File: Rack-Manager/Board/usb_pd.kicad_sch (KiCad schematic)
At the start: 1 part, among them U11 TPS25730D

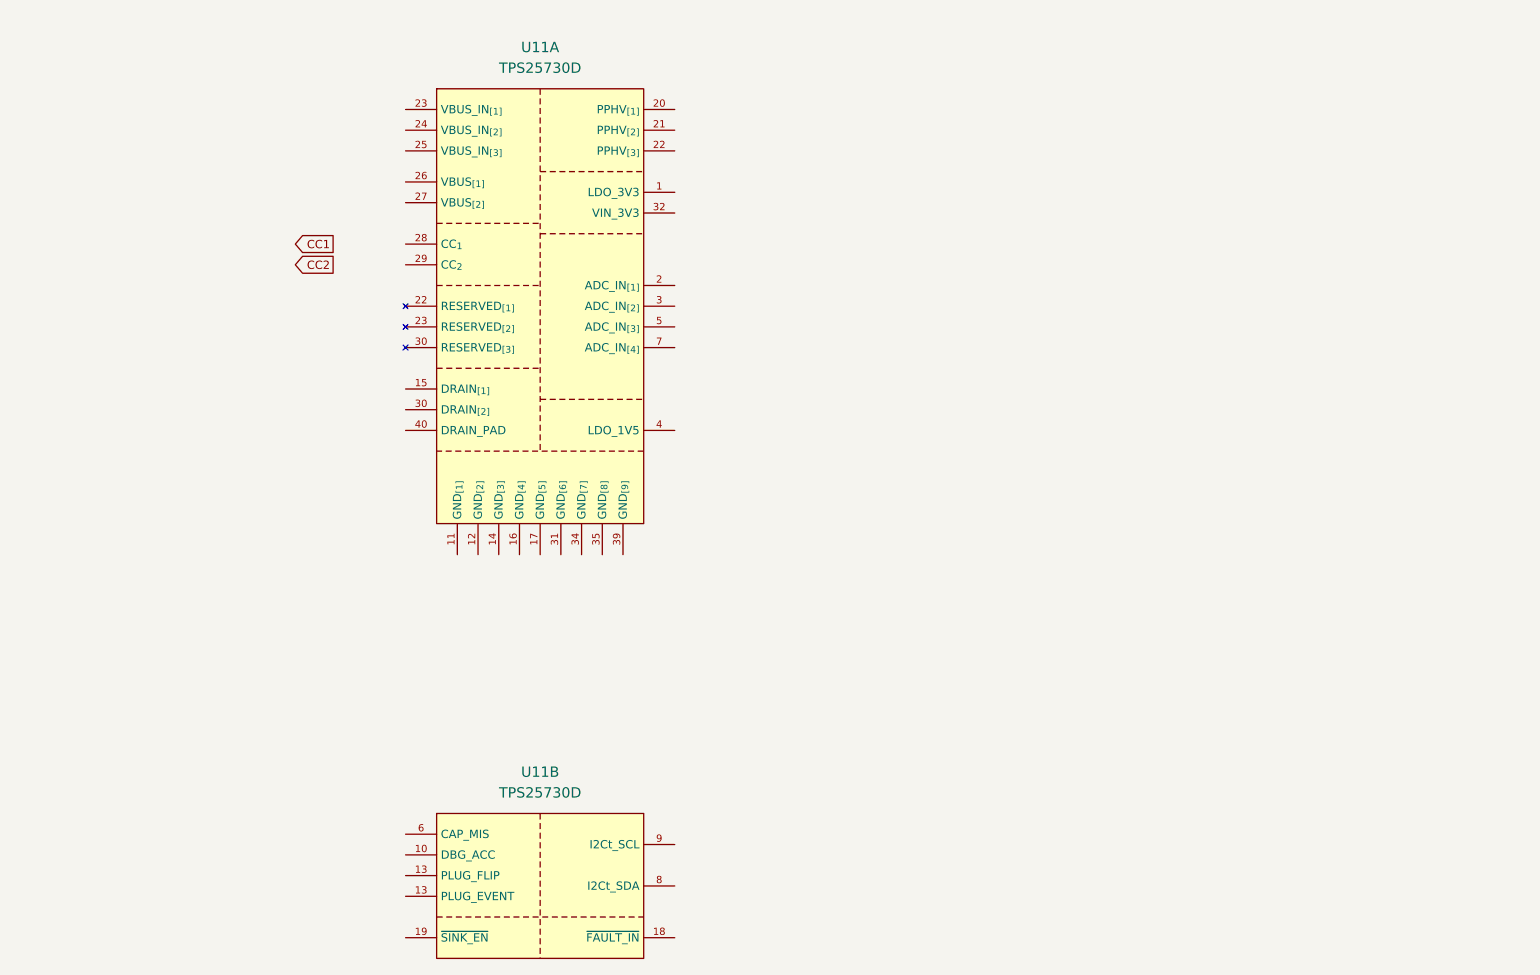
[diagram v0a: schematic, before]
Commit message: Added dvdt cap on eFuses and choose PD standalone sink controller
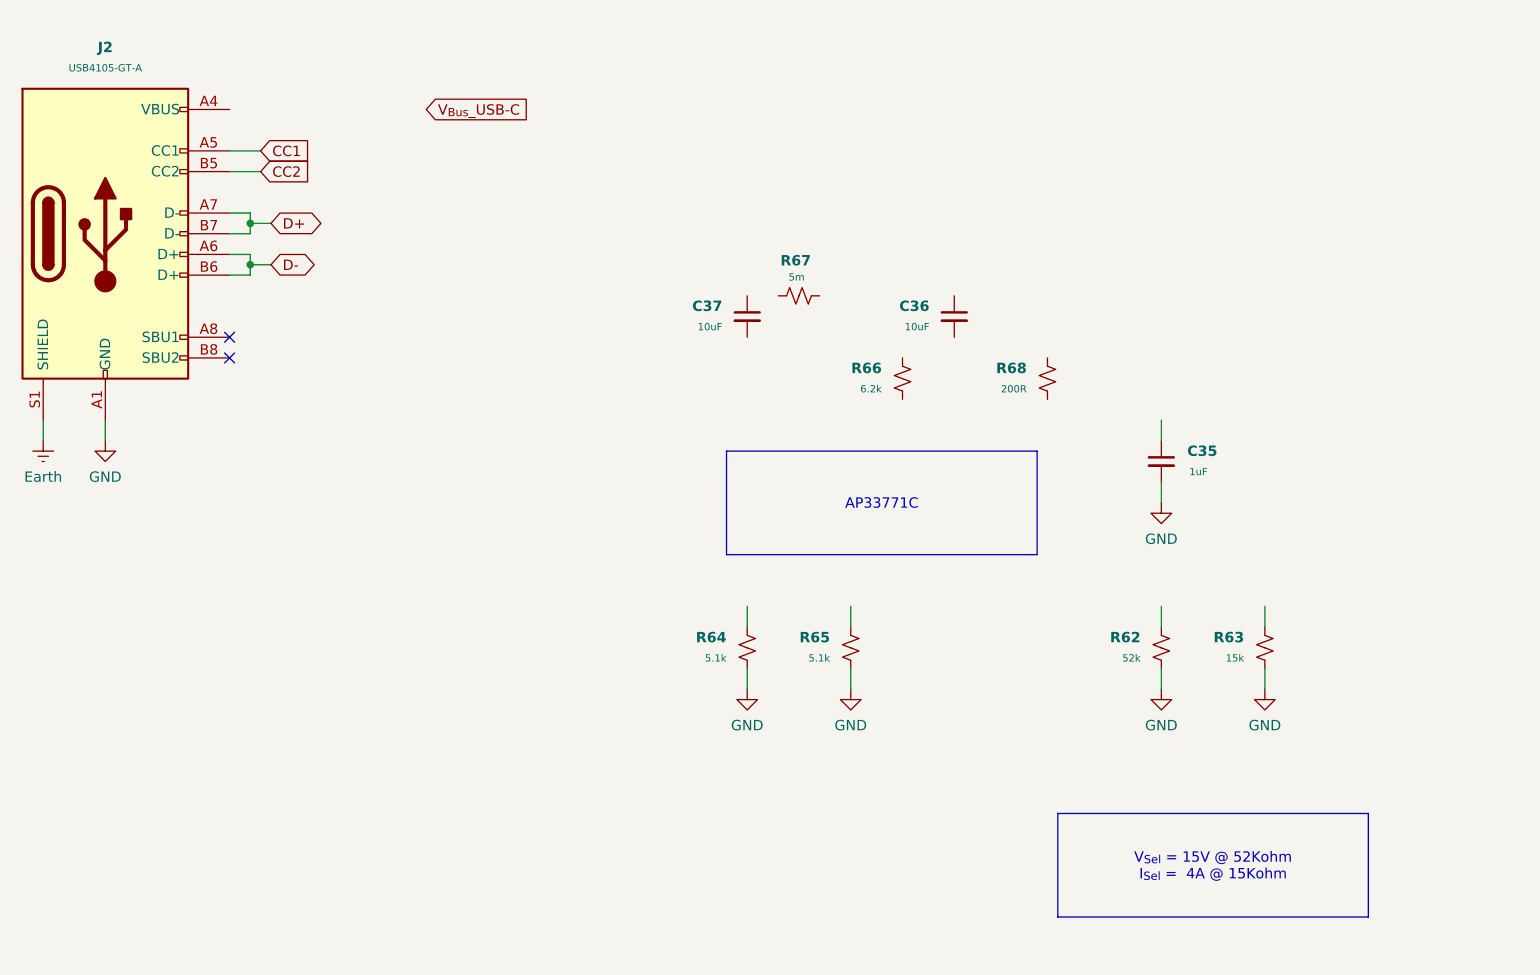
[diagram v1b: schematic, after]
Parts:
- removed U11: TPS25730D, Texas Instruments:REF0038A, symbol Texas Instruments:TPS25730D
- added C35: 1uF, Capacitor_SMD:C_0402_1005Metric, symbol Device:C_Small
- added C36, C37: 10uF, Capacitor_SMD:C_0805_2012Metric, symbol Device:C_Small
- added J2: USB4105-GT-A, Connector_USB:USB_C_Receptacle_GCT_USB4105-xx-A_16P_TopMnt_Horizontal, symbol Connector:USB_C_Receptacle_USB2.0_16P
- added R62: 52k, Resistor_SMD:R_0402_1005Metric, symbol Device:R_Small_US
- added R63: 15k, Resistor_SMD:R_0402_1005Metric, symbol Device:R_Small_US
- added R64, R65: 5.1k, Resistor_SMD:R_0402_1005Metric, symbol Device:R_Small_US
- added R66: 6.2k, Resistor_SMD:R_0402_1005Metric, symbol Device:R_Small_US
- added R67: 5m, symbol Device:R_Small_US
- added R68: 200R, symbol Device:R_Small_US
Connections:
- net CC1: now also J2.A5 (CC1)
- net CC2: now also J2.B5 (CC2)
- new net: J2.A4 (VBUS), J2.A9 (VBUS), J2.B4 (VBUS), J2.B9 (VBUS)
- new net D+: J2.A7 (D-), J2.B7 (D-)
- new net D-: J2.A6 (D+), J2.B6 (D+)
- new net Earth: J2.S1 (SHIELD)
- new net GND: C35.2, J2.A1 (GND), J2.A12 (GND), J2.B1 (GND), J2.B12 (GND), R62.2, R63.2, R64.2, R65.2
- no-connect marks 0 -> 2

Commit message: Updated .gitignore, added USB-C sink controller and fix earth on GDT
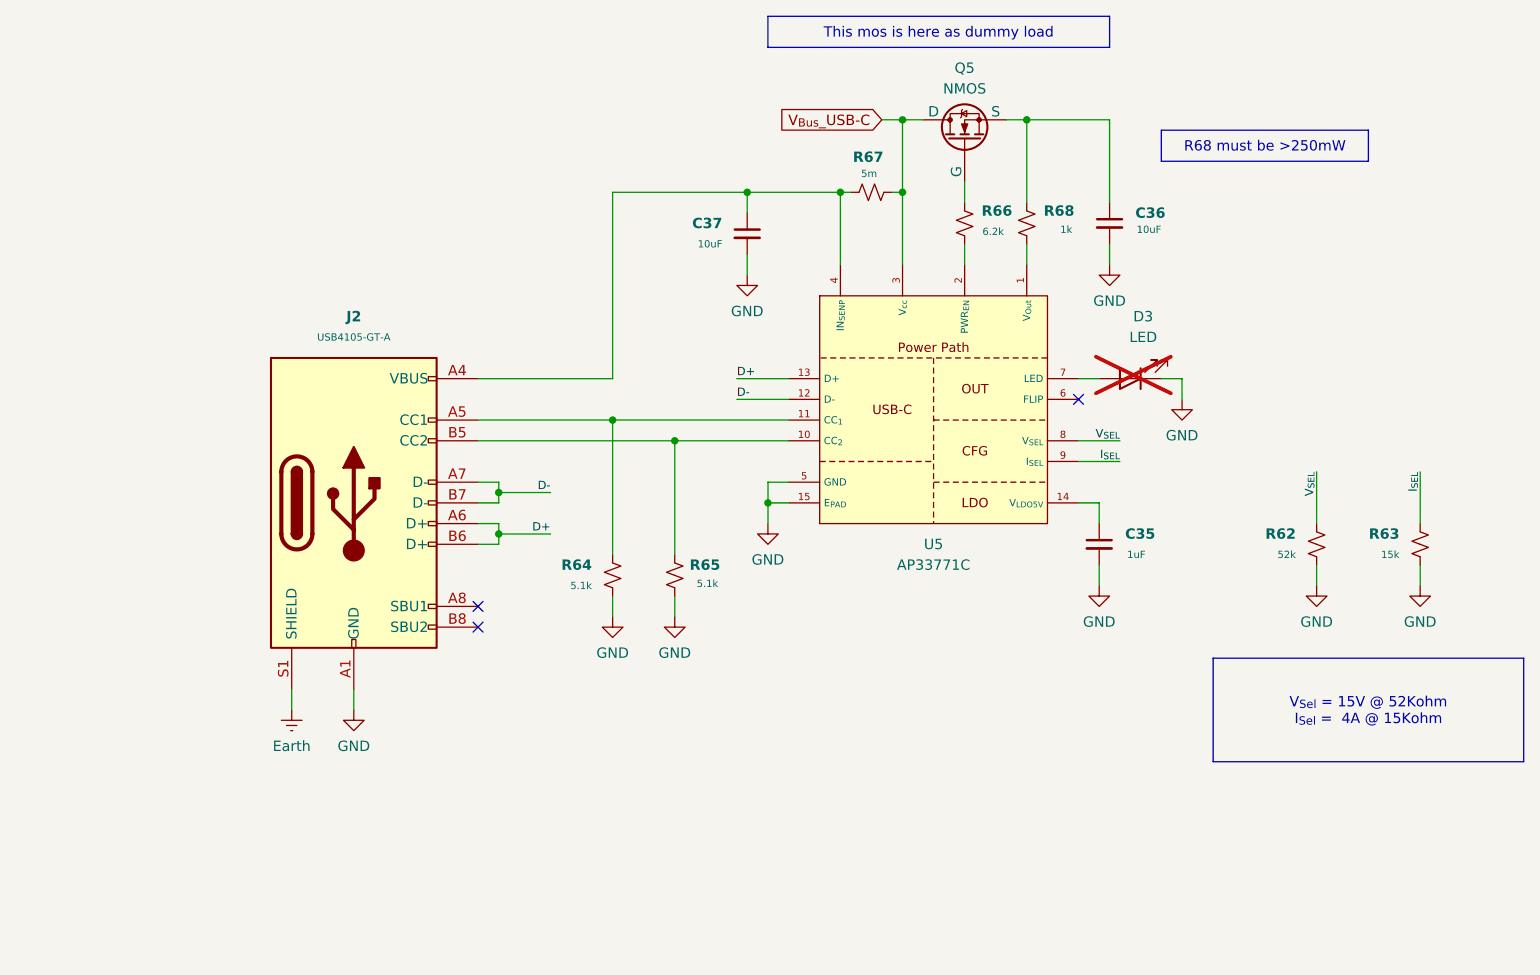
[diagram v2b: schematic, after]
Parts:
- added D3: LED, LED_SMD:LED_0603_1608Metric, symbol Device:LED
- added Q5: NMOS, Package_TO_SOT_SMD:SOT-23-3, symbol Simulation_SPICE:NMOS
- added U5: AP33771C, Package_DFN_QFN:DFN-14-1EP_3x3mm_P0.4mm_EP1.78x2.35mm, symbol Diodes:AP33771C
- R67: footprint (none) -> Resistor_SMD:R_0805_2012Metric
- R68: value 200R -> 1k; footprint (none) -> Resistor_SMD:R_0805_2012Metric
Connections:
- net CC1 is gone; now on an unnamed net: J2.A5 (CC1)
- net CC2 is gone; now on an unnamed net: J2.B5 (CC2)
- net D+: now also J2.A6 (D+), J2.B6 (D+), U5.13 (D+); no longer J2.A7 (D-), J2.B7 (D-)
- net D-: now also J2.A7 (D-), J2.B7 (D-), U5.12 (D-); no longer J2.A6 (D+), J2.B6 (D+)
- net GND: now also C36.2, C37.2, D3.1 (K), U5.15 (E_{PAD}), U5.5 (GND)
- net V_{Bus}_USB-C: now also R67.2, Q5.1 (D), U5.3 (V_{cc})
- net at R66.1: now also Q5.2 (G)
- net at R66.2: now also U5.2 (PWR_{EN})
- net at C37.1: now also J2.A4 (VBUS), J2.A9 (VBUS), J2.B4 (VBUS), J2.B9 (VBUS), R67.1, U5.4 (IN_{SENP})
- net V_{SEL}: now reaches R62.1
- net V_{SEL}: now also U5.8 (V_{SEL})
- net at C35.1: now also U5.14 (V_{LDO5V})
- net at R64.1: now also U5.11 (CC_{1})
- net at C36.1: now also R68.1, Q5.3 (S)
- net I_{SEL}: now reaches R63.1
- net I_{SEL}: now also U5.9 (I_{SEL})
- net at R68.2: now also U5.1 (V_{Out})
- net at R65.1: now also U5.10 (CC_{2})
- new net: D3.2 (A), U5.7 (LED)
- no-connect marks 2 -> 3
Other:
- moved on the sheet: C35, C36, C37, J2, R62, R63, R64, R65, R66, R67, R68

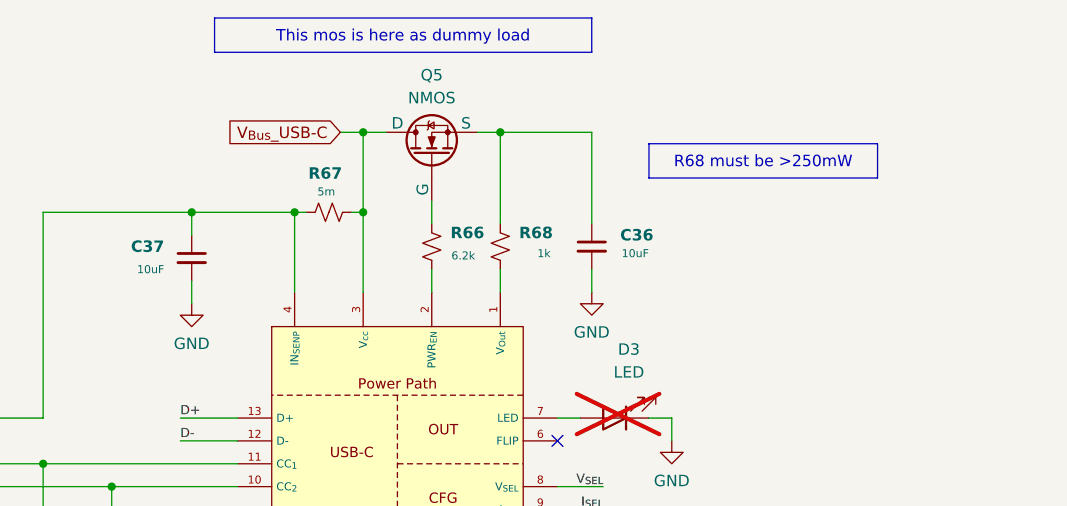
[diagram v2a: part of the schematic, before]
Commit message: Fixed volteage divider for fan tachometer and fixed other pull-x and divider for the microcontroller
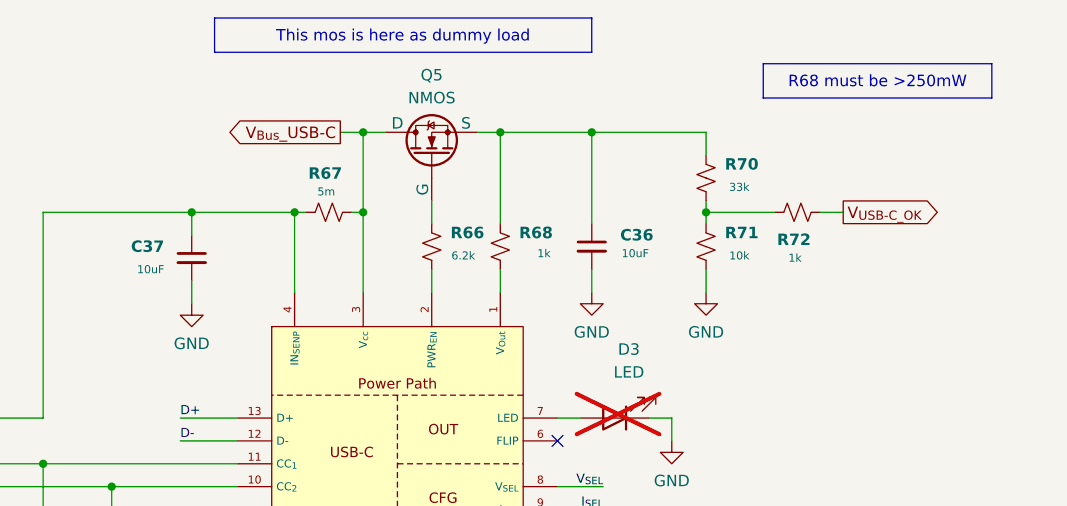
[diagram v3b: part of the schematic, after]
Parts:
- added R70: 33k, Resistor_SMD:R_0402_1005Metric, symbol Device:R_Small_US
- added R71: 10k, Resistor_SMD:R_0402_1005Metric, symbol Device:R_Small_US
- added R72: 1k, Resistor_SMD:R_0402_1005Metric, symbol Device:R_Small_US
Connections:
- net GND: now also R71.2
- net at C36.1, Q5.3 (S), R68.1: now also R70.1
- new net: R70.2, R71.1, R72.1
- new net V_{USB-C_OK}: R72.2

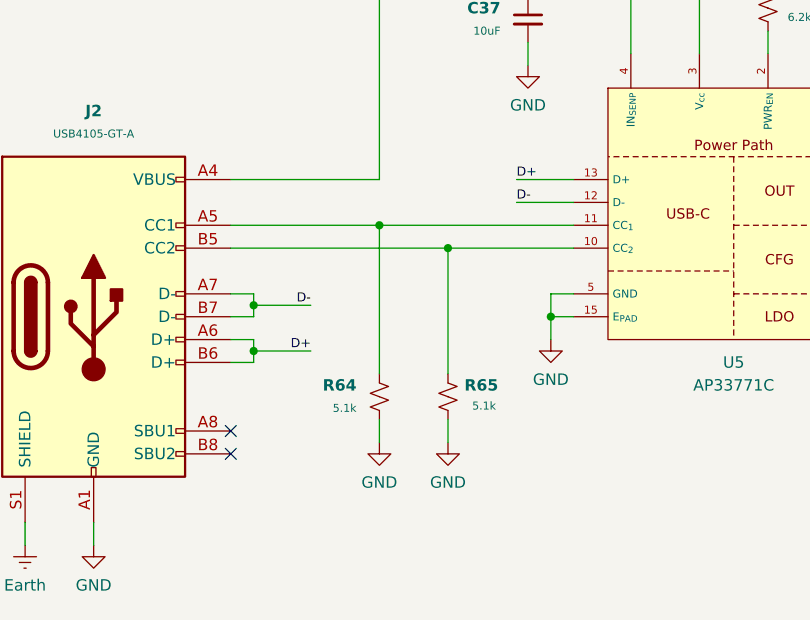
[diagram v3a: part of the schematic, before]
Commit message: Added MCU, Fixed USB-C PD Ideal Diode bug and updated the todo notes
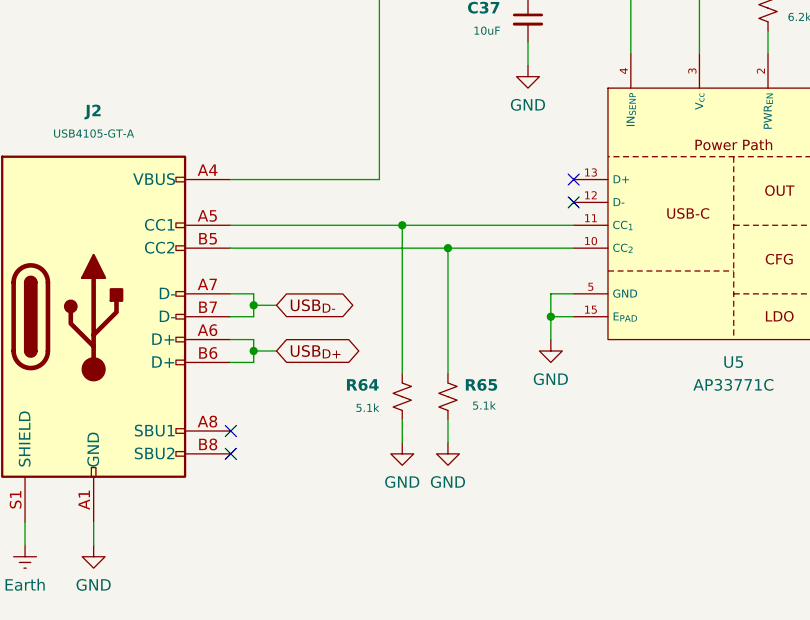
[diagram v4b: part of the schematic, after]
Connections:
- net D+ renamed USB_{D+}
- net USB_{D+}: no longer U5.13 (D+)
- net D- renamed USB_{D-}
- net USB_{D-}: no longer U5.12 (D-)
- no-connect marks 3 -> 5
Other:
- moved on the sheet: R64
